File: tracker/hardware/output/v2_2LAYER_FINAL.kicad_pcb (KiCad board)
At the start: 2 copper layers, 50 x 40 mm, 17 parts, among them U1 ESP32-C3, U2 LR2021F33, U3 MAX-M10S, U4 TPS7A02

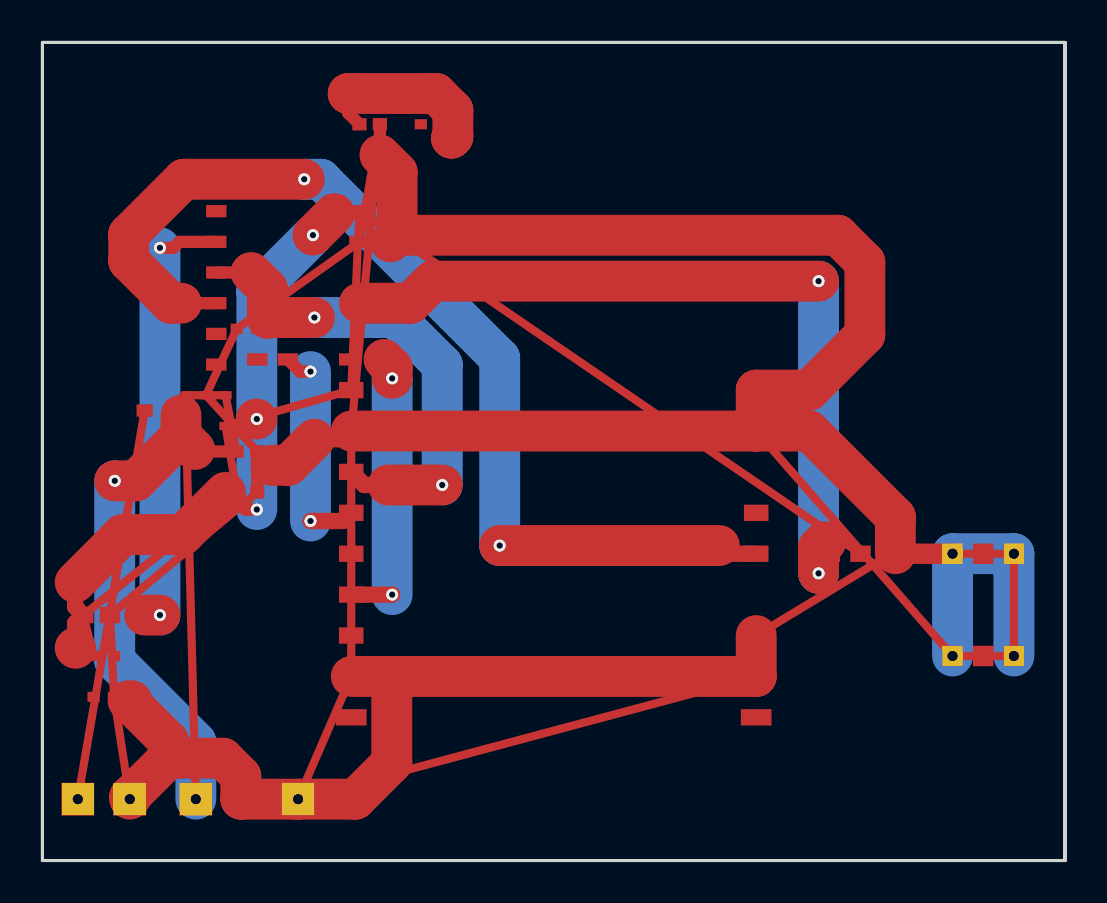
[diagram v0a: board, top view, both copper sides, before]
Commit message: fix: V2-ADC 2-layer FINAL — outline+gerbers, 0 violations, 16 unconnected (power nets)
2-layer board with signal routing complete. 16 unconnected pads are all
power nets (3V3/GND/VCAP) that need manual routing in KiCad GUI or
will be solved by the 4-layer redesign with internal power planes.
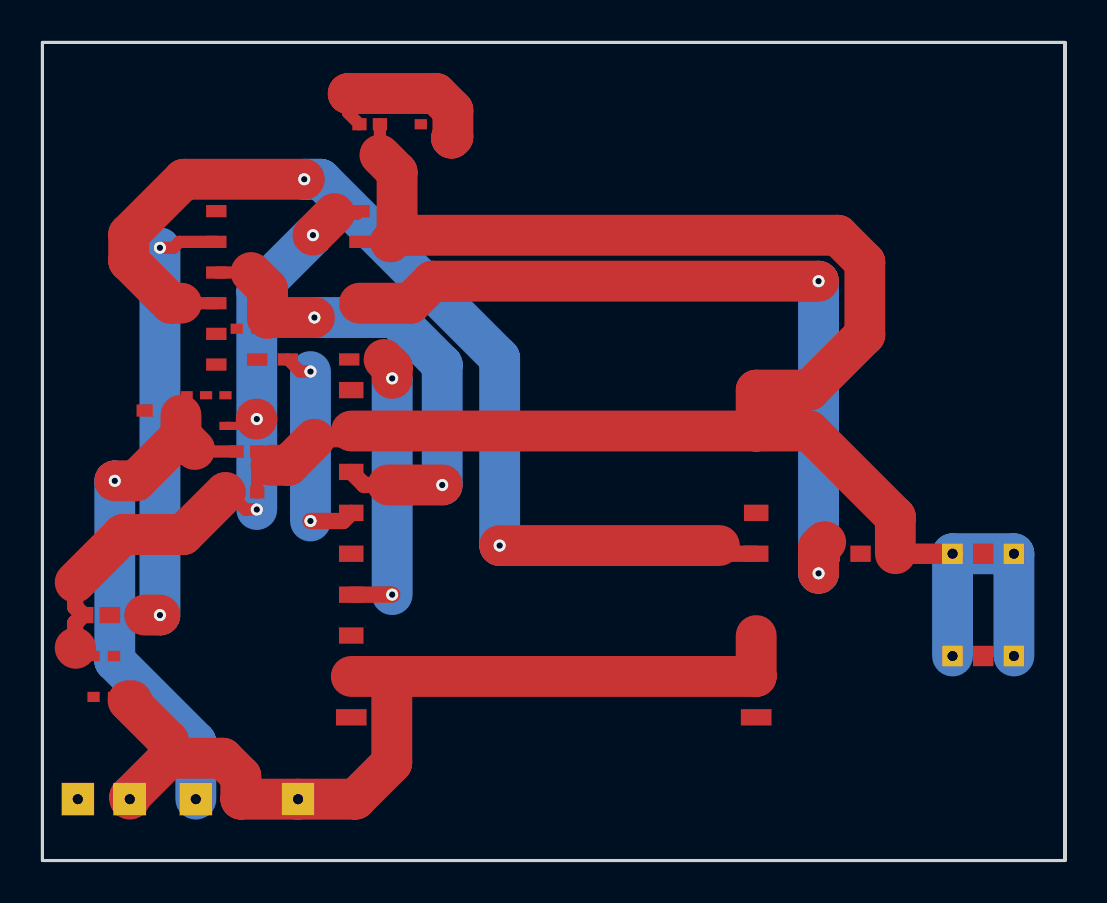
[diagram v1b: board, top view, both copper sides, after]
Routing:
- net GND: track 281.3 -> 143.3 mm
- net 3V3: track 94.9 -> 35.1 mm
- net VCAP: track 51.0 -> 26.5 mm
- net SOLAR_IN: track 19.3 -> 0.00 mm
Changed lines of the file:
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@@
-	)
-	(segment
-		(start 2 28)
-		(end 9.5 22)
-		(width 0.4)
-		(layer "F.Cu")
-		(net 1)
 	)
 	(segment
@@
 	)
 	(segment
-		(start 8.95 18.75)
-		(end 15.1 17)
-		(width 0.4)
-		(layer "F.Cu")
-		(net 1)
-	)
-	(segment
 		(start 9.5 22)
 		(end 9.5 22.4134)
@@
 	)
 	(segment
-		(start 2.5 30)
-		(end 2 28)
-		(width 0.4)
-		(layer "F.Cu")
-		(net 1)
-	)
-	(segment
 		(start 1.5998 26.3981)
 		(end 1.5998 27.5998)
@@
 	)
 	(segment
-		(start 15.1 17)
-		(end 15.5 8.25)
-		(width 0.4)
-		(layer "F.Cu")
-		(net 1)
-	)
-	(segment
-		(start 15.5 8.25)
-		(end 40 25)
-		(width 0.4)
-		(layer "F.Cu")
-		(net 1)
-	)
-	(segment
 		(start 1.5998 28.4002)
 		(end 2 28)
@@
 		(net 1)
 	)
-	(segment
-		(start 9.5 22)
-		(end 8.95 18.75)
-		(width 0.4)
-		(layer "F.Cu")
-		(net 1)
-	)
 	(via
 		(at 13.2268 9.4217)
@@
 	)
 	(segment
-		(start 16.5 4)
-		(end 15.1 19)
-		(width 0.4)
-		(layer "F.Cu")
-		(net 2)
-	)
-	(segment
 		(start 4.375 32.3748)
 		(end 6.1558 34.1556)
@@
 	)
 	(segment
-		(start 12.5 37)
-		(end 34.9 31)
-		(width 0.4)
-		(layer "F.Cu")
-		(net 2)
-	)
-	(segment
 		(start 40.2118 14.2882)
 		(end 40.2118 10.7452)
@@
 		(end 15.1 31)
 		(width 2)
-		(layer "F.Cu")
-		(net 2)
-	)
-	(segment
-		(start 3.5 32)
-		(end 3.3 28)
-		(width 0.4)
-		(layer "F.Cu")
-		(net 2)
-	)
-	(segment
-		(start 15.1 31)
-		(end 12.5 37)
-		(width 0.4)
-		(layer "F.Cu")
-		(net 2)
-	)
-	(segment
-		(start 41.5 25)
-		(end 44.5 25)
-		(width 0.4)
-		(layer "F.Cu")
-		(net 2)
-	)
-	(segment
-		(start 15.1 19)
-		(end 15.1 31)
-		(width 0.4)
 		(layer "F.Cu")
 		(net 2)
@@
 	)
 	(segment
-		(start 4.27 37)
-		(end 3.5 32)
-		(width 0.4)
-		(layer "F.Cu")
-		(net 2)
-	)
-	(segment
-		(start 9.5 14)
-		(end 15.5 9.75)
-		(width 0.4)
-		(layer "F.Cu")
-		(net 2)
-	)
-	(segment
-		(start 47.5 30)
-		(end 44.5 30)
-		(width 0.4)
-		(layer "F.Cu")
-		(net 2)
-	)
-	(segment
 		(start 9.7 37)
 		(end 9.7 35.874)
@@
 		(end 10.5 20)
 		(width 0.5998)
-		(layer "F.Cu")
-		(net 2)
-	)
-	(segment
-		(start 8 17.25)
-		(end 9.5 14)
-		(width 0.4)
 		(layer "F.Cu")
 		(net 2)
@@
 	)
 	(segment
-		(start 3.3 28)
-		(end 10.5 22)
-		(width 0.4)
-		(layer "F.Cu")
-		(net 2)
-	)
-	(segment
 		(start 14.7002 19.3998)
 		(end 15.1 19)
@@
 	(segment
 		(start 34.9 31)
-		(end 34.9 29)
-		(width 0.4)
-		(layer "F.Cu")
-		(net 2)
-	)
-	(segment
-		(start 34.9 31)
 		(end 17.0819 31)
 		(width 2)
-		(layer "F.Cu")
-		(net 2)
-	)
-	(segment
-		(start 47.5 25)
-		(end 47.5 30)
-		(width 0.4)
 		(layer "F.Cu")
 		(net 2)
@@
 	)
 	(segment
-		(start 10.5 20)
-		(end 8 17.25)
-		(width 0.4)
-		(layer "F.Cu")
-		(net 2)
-	)
-	(segment
 		(start 4.1876 32.1874)
 		(end 4.375 32.1874)
@@
 		(end 8.8243 34.9983)
 		(width 2)
-		(layer "F.Cu")
-		(net 2)
-	)
-	(segment
-		(start 34.9 19)
-		(end 34.9 17)
-		(width 0.4)
 		(layer "F.Cu")
 		(net 2)
@@
 	)
 	(segment
-		(start 10.5 22)
-		(end 10.5 20)
-		(width 0.4)
-		(layer "F.Cu")
-		(net 2)
-	)
-	(segment
-		(start 44.5 30)
-		(end 34.9 19)
-		(width 0.4)
-		(layer "F.Cu")
-		(net 2)
-	)
-	(segment
-		(start 34.9 29)
-		(end 41.5 25)
-		(width 0.4)
-		(layer "F.Cu")
-		(net 2)
-	)
-	(segment
 		(start 17.3412 9.4277)
 		(end 17.0189 9.75)
@@
 		(end 40.2118 14.2882)
 		(width 2)
-		(layer "F.Cu")
-		(net 2)
-	)
-	(segment
-		(start 44.5 25)
-		(end 47.5 25)
-		(width 0.4)
-		(layer "F.Cu")
-		(net 2)
-	)
-	(segment
-		(start 15.5 9.75)
-		(end 16.5 4)
-		(width 0.4)
 		(layer "F.Cu")
 		(net 2)
@@
 	)
 	(segment
-		(start 7 18)
-		(end 7.5 37)
-		(width 0.4)
-		(layer "F.Cu")
-		(net 13)
-	)
-	(segment
 		(start 9.5 20)
 		(end 7.8501 20)
@@
 		(end 7 18)
 		(width 0.5998)
-		(layer "F.Cu")
-		(net 13)
-	)
-	(segment
-		(start 8.95 17.25)
-		(end 7.05 17.25)
-		(width 0.4)
 		(layer "F.Cu")
 		(net 13)
@@
 		(net 13)
 	)
-	(segment
-		(start 9.5 20)
-		(end 8.95 17.25)
-		(width 0.4)
-		(layer "F.Cu")
-		(net 13)
-	)
-	(segment
-		(start 7.05 17.25)
-		(end 7 18)
-		(width 0.4)
-		(layer "F.Cu")
-		(net 13)
-	)
 	(via
 		(at 3.5358 21.4352)
@@
 	)
 	(segment
-		(start 1.73 37)
-		(end 5 18)
-		(width 0.4)
-		(layer "F.Cu")
-		(net 14)
-	)
-	(segment
